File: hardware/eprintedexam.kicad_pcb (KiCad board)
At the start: 2 copper layers, 103 x 98.5 mm, 41 parts, among them J1 Conn_01x04, J2 Conn_01x08, Q1 2N7002, Q2 2N7002, Q3 2N7002, Q4 2N7002, Q5 2N7002, Q6 2N7002, SW1 SW_Push, SW2 SW_Push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

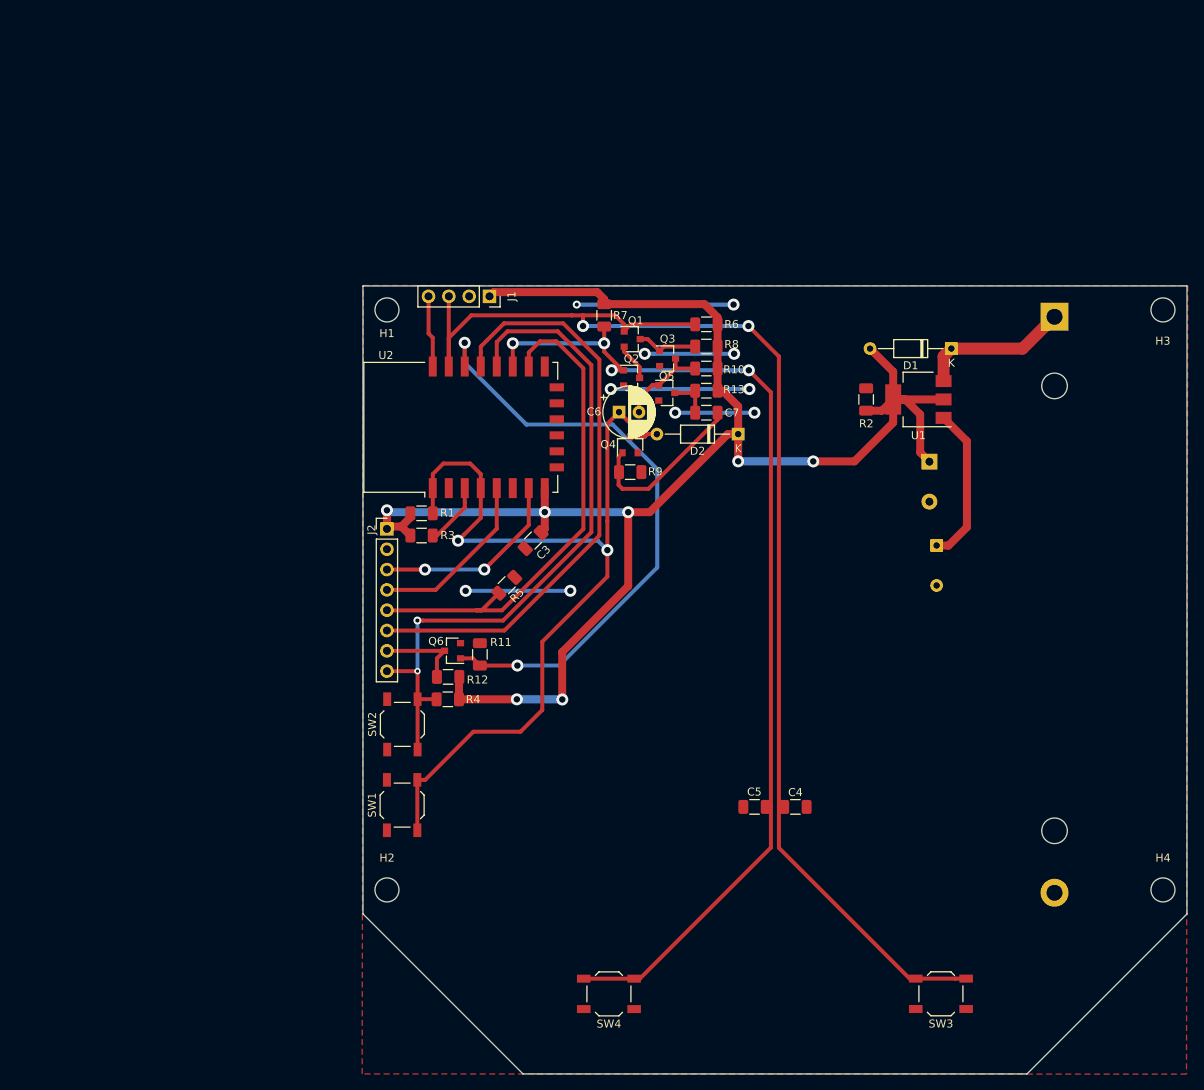
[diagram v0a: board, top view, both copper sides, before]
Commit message: removed simplified version
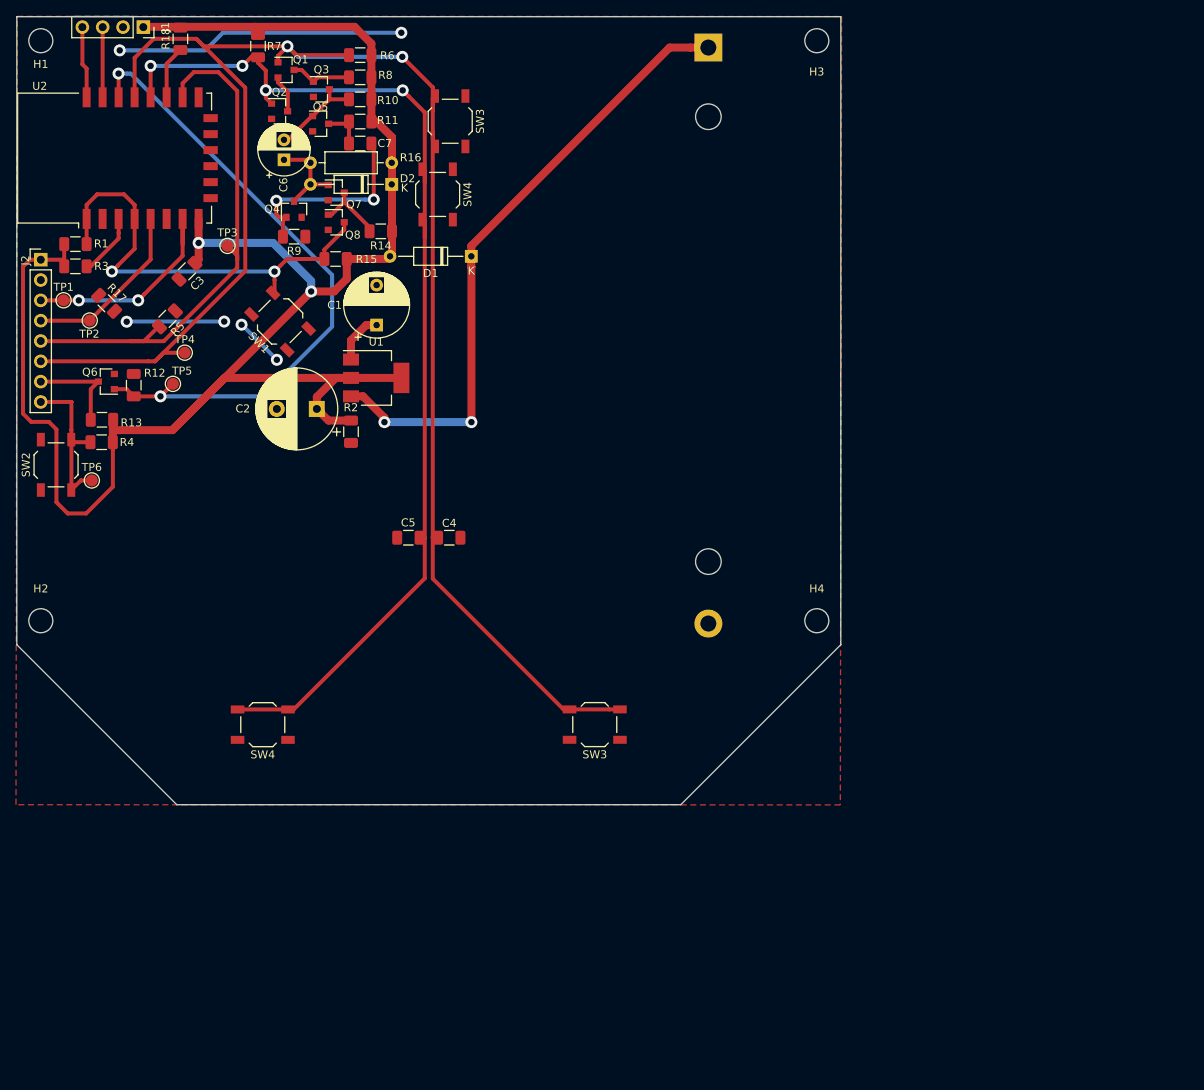
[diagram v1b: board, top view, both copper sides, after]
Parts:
- removed the SW3 at (163.5, 134.6)
- removed the SW4 at (122.0, 134.6)
- added Q7: 2N7002, Package_TO_SOT_SMD:SOT-23, F.Cu at (87.9, 34.5)
- added Q8: 2N7002, Package_TO_SOT_SMD:SOT-23, F.Cu at (87.9, 38.2)
- added R14: 18k, Resistor_SMD:R_1206_3216Metric, F.Cu at (93.5, 39.3)
- added R15: 1k, Resistor_SMD:R_1206_3216Metric, F.Cu at (87.8, 42.8)
- added R16: 10k, Resistor_THT:R_Axial_DIN0207_L6.3mm_D2.5mm_P10.16mm_Horizontal, F.Cu at (94.9, 30.7)
- added R17: 0, Resistor_SMD:R_1206_3216Metric, F.Cu at (59.2, 48.3)
- added R18: 10k, Resistor_SMD:R_1206_3216Metric, F.Cu at (68.5, 15.2)
- added SW3: SW_Push, Button_Switch_SMD:SW_SPST_TL3342, F.Cu at (102.2, 25.5)
- added SW3: SW_Push, Button_Switch_SMD:SW_SPST_TL3342, F.Cu at (120.2, 101.0)
- added SW4: SW_Push, Button_Switch_SMD:SW_SPST_TL3342, F.Cu at (100.6, 34.7)
- added SW4: SW_Push, Button_Switch_SMD:SW_SPST_TL3342, F.Cu at (78.8, 101.0)
- added TP1: TestPoint, TestPoint:TestPoint_Pad_D1.5mm, F.Cu at (53.9, 47.9)
- added TP2: TestPoint, TestPoint:TestPoint_Pad_D1.5mm, F.Cu at (57.1, 50.5)
- added TP3: TestPoint, TestPoint:TestPoint_Pad_D1.5mm, F.Cu at (74.3, 41.1)
- added TP4: TestPoint, TestPoint:TestPoint_Pad_D1.5mm, F.Cu at (69.0, 54.5)
- added TP5: TestPoint, TestPoint:TestPoint_Pad_D1.5mm, F.Cu at (67.5, 58.4)
- added TP6: TestPoint, TestPoint:TestPoint_Pad_D1.5mm, F.Cu at (57.4, 70.4)
- C1, C2: moved to F.Cu
- R11: value 10k -> 680k
- R13: value 680k -> 10k
- R6, R7: value 10k -> 5k
- moved C2 76.9 mm to (85.5, 61.5), turned to 180 degrees
- moved R13 75.6 mm to (58.6, 62.9)
- moved C1 75.2 mm to (93.0, 51.0), turned to 90 degrees
- moved R11 68.3 mm to (90.9, 25.6), turned to 180 degrees
- moved U1 67.8 mm to (92.9, 57.6), turned to 0 degrees
- moved R2 64.5 mm to (89.8, 64.3), turned to 270 degrees
- moved SW1 62.3 mm to (80.9, 50.6), turned to 135 degrees
- moved D1 61.1 mm to (104.8, 42.4)
- moved Q2 55.2 mm to (80.8, 24.3)
- moved C4 54.8 mm to (102.1, 77.6)
- moved H4 54.8 mm to (148.0, 88.0)
- moved BT1 54.8 mm to (134.4, 16.3)
- moved H1 54.8 mm to (51.0, 15.5)
- moved H2 54.8 mm to (51.0, 88.0)
- moved H3 54.8 mm to (148.0, 15.5)
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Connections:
- C6 pad 1: nrst -> Net-(C6-Pad1)
- D2 pad 2: nrst -> Net-(C6-Pad1)
- J1 pad 3: nxt -> Net-(J1-Pad3)
- J2 pad 6: spi-dc -> nxt
- J2 pad 8: spi-busy,flash -> prv
- Q4 pad 3: nrst -> Net-(C6-Pad1)
- R11 pad 1: spi-rst -> VCC
- R11 pad 2: GND -> Net-(C7-Pad1)
- R12 pad 1: VCC -> spi-rst
- R12 pad 2: spi-nrst -> GND
- R13 pad 2: Net-(C7-Pad1) -> spi-nrst
- R4 pad 2: spi-busy,flash -> prv
- R6 pad 1: nxt -> VCC
- R6 pad 2: VCC -> nxt
- SW2 pad 2: spi-busy,flash -> prv
- U2 pad 17: prv -> Net-(R18-Pad1)
- U2 pad 18: spi-busy,flash -> prv
- U2 pad 19: spi-dc -> nxt
- U2 pad 21: nxt -> Net-(J1-Pad3)
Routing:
- net spi-busy,flash: track 86.8 -> 0.00 mm, vias 2 -> 0
- net spi-dc: track 73.9 -> 0.00 mm
- net Net-(BT1-Pad1): track 19.0 -> 78.7 mm, vias 0 -> 2
- net nrst: track 114.6 -> 57.1 mm
- net nxt: track 165.7 -> 217.5 mm
- net VCC: track 206.9 -> 240.6 mm, vias 7 -> 2
- net prv: track 131.2 -> 159.0 mm
- net GND: track 71.1 -> 54.5 mm, vias 10 -> 6
- net Net-(C1-Pad1): track 19.6 -> 6.39 mm
- net Net-(C6-Pad1): track 0.00 -> 11.2 mm
- net Net-(Q7-Pad3): track 0.00 -> 8.81 mm
- net Net-(J1-Pad3): track 0.00 -> 8.68 mm
- net Net-(R18-Pad1): track 0.00 -> 6.62 mm
- net Net-(C7-Pad2): track 21.3 -> 25.7 mm, vias 0 -> 2
- net spi-cs: track 63.1 -> 67.2 mm
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
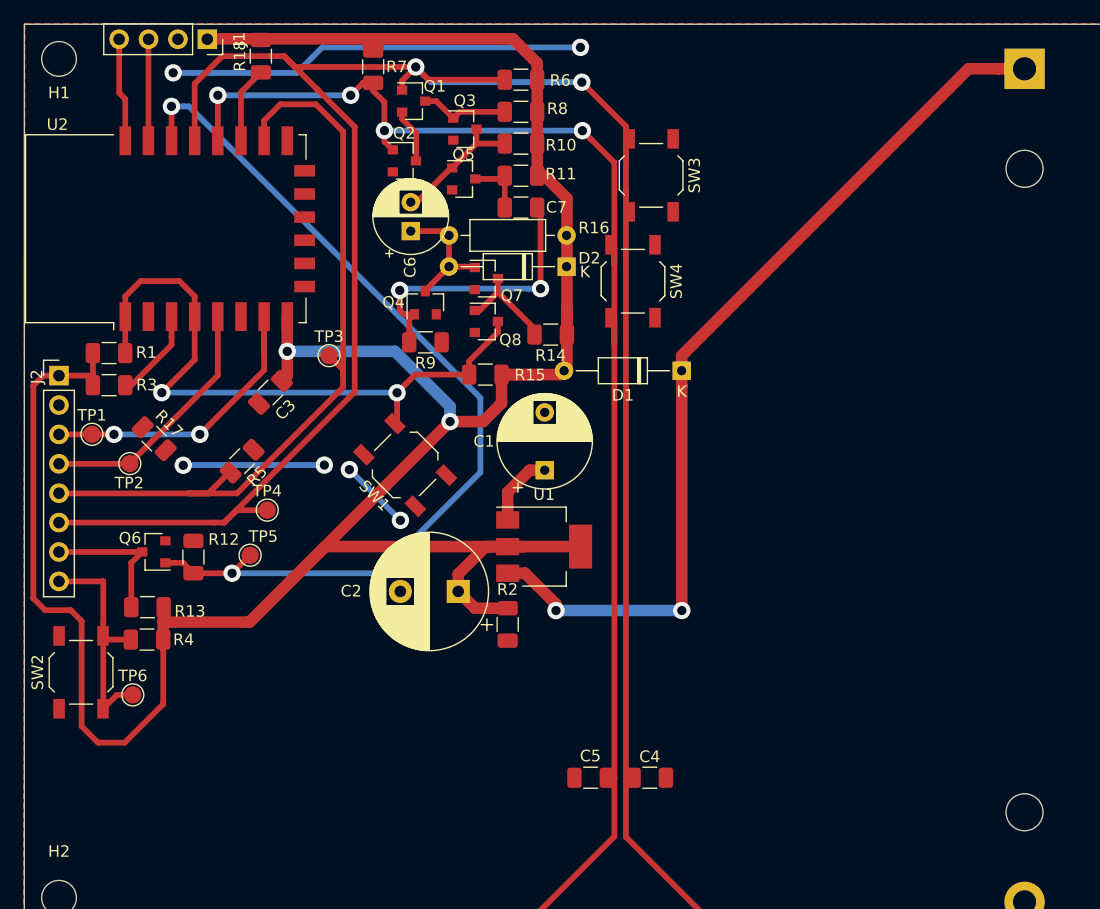
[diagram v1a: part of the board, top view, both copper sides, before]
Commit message: redesing pcb and added isolation mosfets
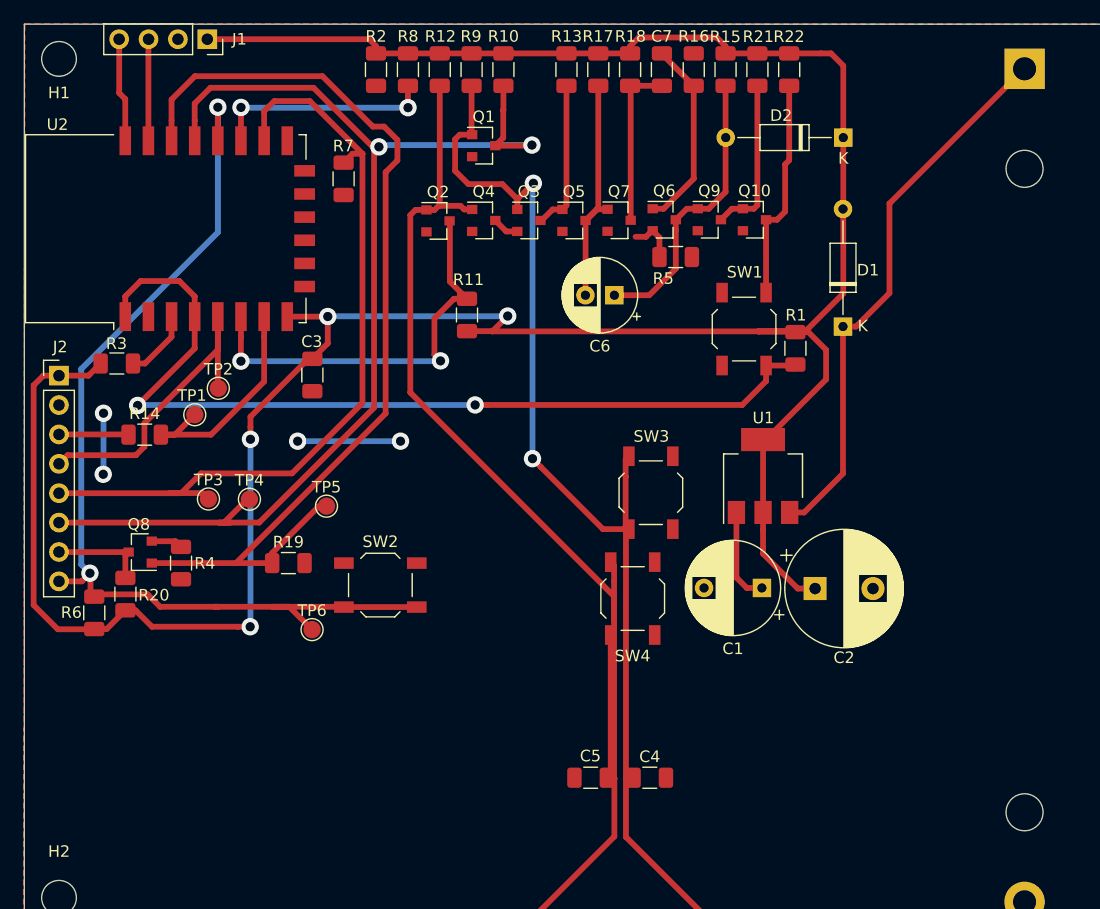
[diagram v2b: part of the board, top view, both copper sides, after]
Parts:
- added Q10: 2N7002, Package_TO_SOT_SMD:SOT-23, F.Cu at (111.1, 29.4)
- added Q9: 2N7002, Package_TO_SOT_SMD:SOT-23, F.Cu at (107.2, 29.4)
- added R19: 10k, Resistor_SMD:R_1206_3216Metric, F.Cu at (70.8, 59.0)
- added R20: 10k, Resistor_SMD:R_1206_3216Metric, F.Cu at (56.7, 61.7)
- added R21: 18k, Resistor_SMD:R_1206_3216Metric, F.Cu at (111.4, 16.4)
- added R22: 1k, Resistor_SMD:R_1206_3216Metric, F.Cu at (114.1, 16.4)
- R10: value 3.3k -> 10k
- R11: value 680k -> 10k
- R12: value 10k -> 5k
- R13: value 10k -> 33k
- R14: value 18k -> 0
- R15: value 1k -> 10k
- R16: value 10k -> 330; footprint Resistor_THT:R_Axial_DIN0207_L6.3mm_D2.5mm_P10.16mm_Horizontal -> Resistor_SMD:R_1206_3216Metric
- R17: value 0 -> 3.3k
- R18: value 10k -> 680k
- R4, R5: value 10k -> 0
- R6, R7: value 5k -> 10k
- R8: value 33k -> 10k
- R9: value 330 -> 5k
- moved R1 59.3 mm to (114.6, 40.5), turned to 270 degrees
- moved R6 59.0 mm to (54.0, 63.4), turned to 90 degrees
- moved R13 58.9 mm to (94.9, 16.4), turned to 90 degrees
- moved Q6 52.6 mm to (103.3, 29.4), turned to 0 degrees
- moved R17 49.9 mm to (97.6, 16.4), turned to 270 degrees
- moved R2 49.3 mm to (78.4, 16.4)
- moved R12 47.2 mm to (83.9, 16.4)
- moved R5 41.4 mm to (104.3, 32.6), turned to 0 degrees
- moved R14 36.1 mm to (58.4, 48.0), turned to 0 degrees
- moved Q8 36.0 mm to (58.0, 58.1), turned to 180 degrees
- moved R15 33.6 mm to (108.6, 16.4), turned to 270 degrees
- moved R18 31.9 mm to (100.4, 16.4), turned to 270 degrees
- moved SW1 31.6 mm to (110.2, 38.8), turned to 90 degrees
- moved C2 30.8 mm to (116.3, 61.2), turned to 0 degrees
- moved SW3 27.4 mm to (102.2, 53.0)
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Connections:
- J2 pad 3: spi-mosi -> Net-(J2-Pad3)
- J2 pad 6: nxt -> spi-dc_nxt-in
- J2 pad 8: prv -> spi-busy,flash
- Q1 pad 2: Net-(Q1-Pad2) -> GND
- Q1 pad 3: Net-(Q1-Pad3) -> spi-dc_nxt-in
- Q2 pad 3: Net-(Q1-Pad2) -> spi-miso_prv-in
- Q3 pad 1: Net-(Q1-Pad3) -> nxt
- Q3 pad 2: GND -> Net-(Q3-Pad2)
- Q3 pad 3: nxt+prv -> Net-(Q3-Pad3)
- Q4 pad 1: Net-(C7-Pad2) -> prv
- Q4 pad 3: Net-(C6-Pad1) -> Net-(Q3-Pad2)
- Q5 pad 1: nxt+prv -> Net-(Q3-Pad3)
- Q5 pad 3: Net-(C7-Pad1) -> nxt+prv
- Q6 pad 1: spi-rst -> Net-(C7-Pad2)
- Q6 pad 3: spi-nrst -> Net-(C6-Pad1)
- Q7 pad 1: Net-(C6-Pad1) -> nxt+prv
- Q7 pad 3: Net-(Q7-Pad3) -> Net-(C7-Pad1)
- Q8 pad 1: Net-(Q7-Pad3) -> spi-rst
- Q8 pad 3: nrst -> spi-nrst
- R10 pad 1: VCC -> spi-dc_nxt-in
- R10 pad 2: nxt+prv -> VCC
- R11 pad 1: VCC -> spi-miso_prv-in
- R11 pad 2: Net-(C7-Pad1) -> VCC
- R12 pad 1: spi-rst -> prv
- R12 pad 2: GND -> VCC
- R13 pad 1: VCC -> Net-(Q3-Pad3)
- R13 pad 2: spi-nrst -> VCC
- R14 pad 1: VCC -> Net-(J2-Pad3)
- R14 pad 2: Net-(Q7-Pad3) -> spi-mosi
- R15 pad 1: nrst -> VCC
- R15 pad 2: VCC -> Net-(C6-Pad1)
- R16 pad 1: VCC -> Net-(C7-Pad2)
- R16 pad 2: Net-(C6-Pad1) -> GND
- R17 pad 1: GND -> VCC
- R17 pad 2: GND -> nxt+prv
- R18 pad 1: Net-(R18-Pad1) -> VCC
- R18 pad 2: VCC -> Net-(C7-Pad1)
- R4 pad 1: VCC -> GND
- R4 pad 2: prv -> GND
- R5 pad 2: spi-cs -> GND
- R6 pad 2: nxt -> spi-busy,flash
- R7 pad 1: prv -> GND
- R7 pad 2: VCC -> spi-cs
- R8 pad 1: Net-(Q1-Pad3) -> Net-(R8-Pad1)
- R9 pad 1: Net-(C7-Pad2) -> VCC
- R9 pad 2: GND -> nxt
- SW2 pad 2: prv -> spi-busy,flash
- TP4 pad 1: nxt -> spi-dc_nxt-in
- TP6 pad 1: prv -> spi-busy,flash
- U2 pad 17: Net-(R18-Pad1) -> Net-(R8-Pad1)
- U2 pad 18: prv -> spi-busy,flash
- U2 pad 19: nxt -> spi-dc_nxt-in
- U2 pad 6: spi-miso -> spi-miso_prv-in
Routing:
- net spi-dc_nxt-in: track 0.00 -> 101.7 mm, vias 0 -> 2
- net nxt: track 217.5 -> 116.6 mm
- net spi-busy,flash: track 0.00 -> 86.5 mm, vias 0 -> 2
- net nrst: track 57.1 -> 99.1 mm
- net spi-miso_prv-in: track 0.00 -> 35.9 mm, vias 0 -> 2
- net GND: track 54.5 -> 21.1 mm, vias 6 -> 4
- net prv: track 159.0 -> 125.9 mm, vias 4 -> 0
- net Net-(BT1-Pad1): track 78.7 -> 48.2 mm, vias 2 -> 0
- net Net-(R8-Pad1): track 0.00 -> 19.2 mm, vias 0 -> 2
- net Net-(Q10-Pad1): track 0.00 -> 14.0 mm
- net Net-(C6-Pad1): track 11.2 -> 25.0 mm
- net Net-(Q3-Pad3): track 0.00 -> 13.0 mm
- net nxt+prv: track 11.5 -> 20.9 mm
- net Net-(C7-Pad2): track 25.7 -> 16.6 mm, vias 2 -> 0
- net Net-(C7-Pad1): track 5.41 -> 14.4 mm
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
